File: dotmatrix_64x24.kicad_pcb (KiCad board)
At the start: 2 copper layers, 180 x 100 mm, 369 parts, among them CON1 BARREL_JACK, P1 CONN_01X09, P2 CONN_01X09, P3 CONN_01X04, P4 CONN_01X03, P5 USB_OTG, P6 CONN_01X03, Q1 NJL7302L-F3, SW1 SW_PUSH_SMALL_H, SW2 SW_PUSH_SMALL_H, SW3 SW_PUSH_SMALL_H, SW4 SW_PUSH_SMALL_H, SW5 SW_PUSH_SMALL_H, SW6 SW_PUSH_SMALL_H, SW7 SW_PUSH_SMALL_H, SW8 SW_PUSH_SMALL_H, U1 WROOM-02, U10 LED1642GW, U11 LED1642GW, U12 AE-BME280, U13 OKL-T/6-W5, U14 NJU7223, U15 DS1307, U16 CH340G, U2 74HC595-alt-vdd, U3 TD62783, U4 74HC595-alt-vdd, U5 TD62783, U6 LED1642GW, U7 74HC595-alt-vdd, U8 TD62783, U9 LED1642GW, X1 CRYSTAL_SMD, Y1 12MHz

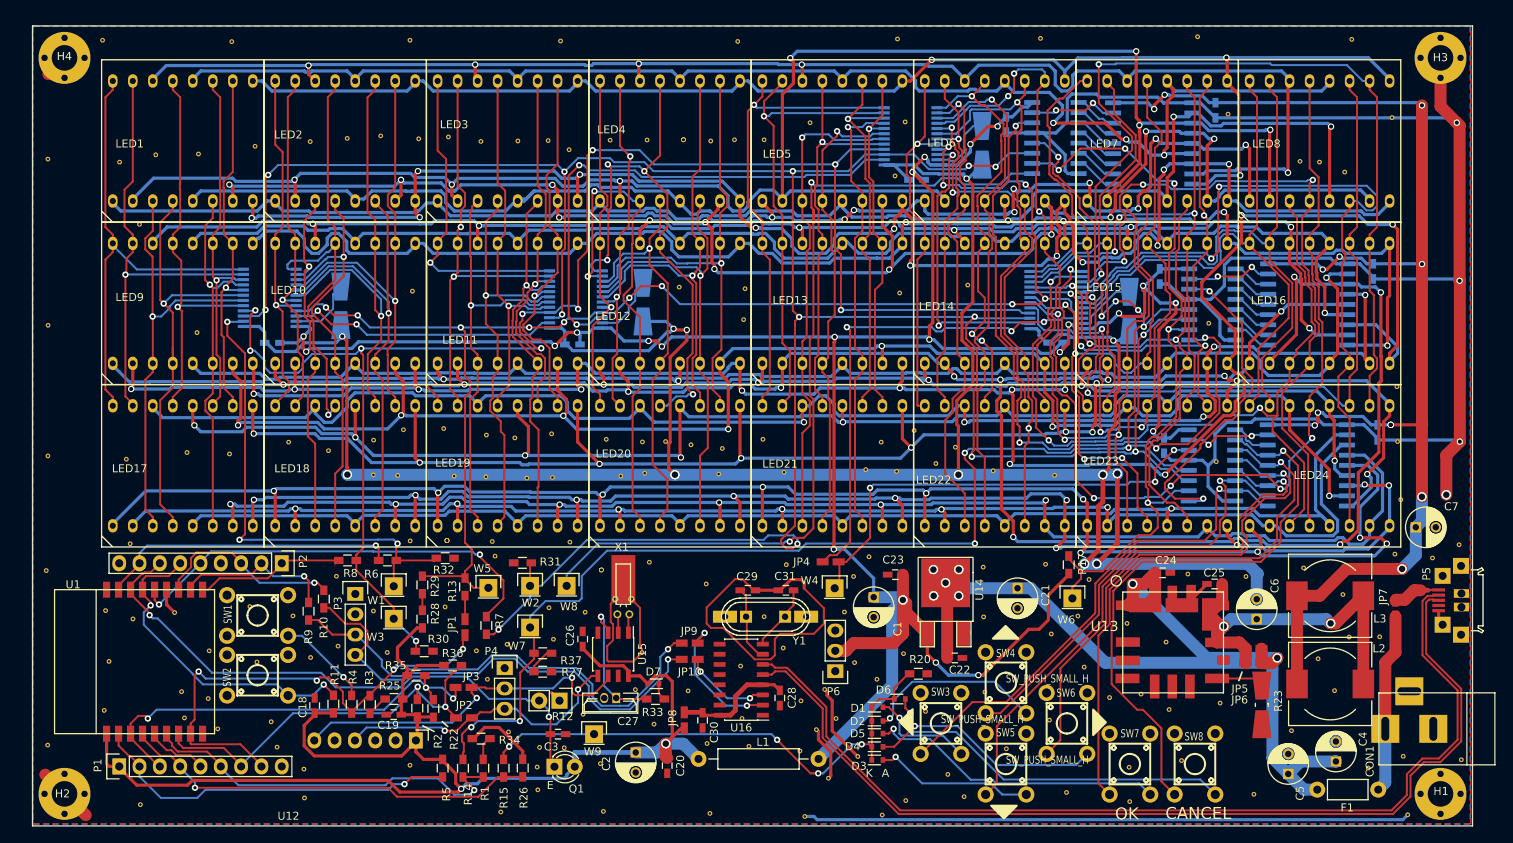
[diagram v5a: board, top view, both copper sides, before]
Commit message: Added IR remote control functionality
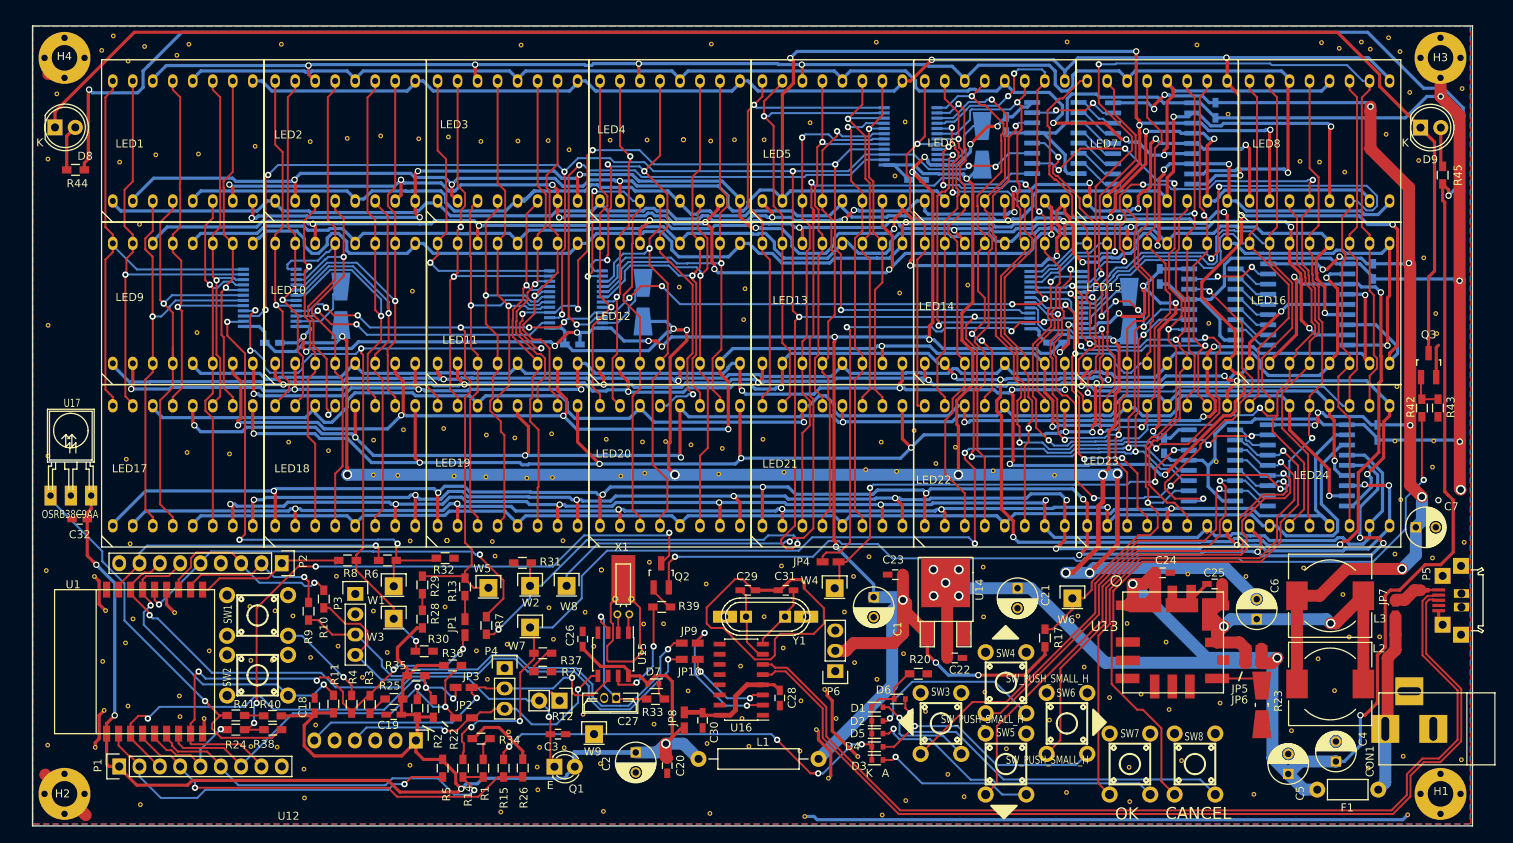
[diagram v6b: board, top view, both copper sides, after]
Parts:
- removed the REF** at (157.6, 13.4)
- removed the REF** at (138.0, 13.6)
- removed the REF** at (120.1, 13.6)
- removed the REF** at (100.2, 13.9)
- removed the REF** at (78.0, 13.9)
- removed the REF** at (59.2, 13.8)
- removed the REF** at (36.9, 14.0)
- removed the REF** at (87.4, 95.0)
- removed the REF** at (34.0, 96.1)
- removed the REF** at (30.6, 95.2)
- removed the REF** at (139.3, 88.0)
- removed the REF** at (144.1, 81.2)
- removed the REF** at (138.6, 79.3)
- added C32: 1u, Capacitors_SMD:C_0603_HandSoldering, F.Cu at (17.9, 73.7)
- added D8: Led_Small, LEDs:LED-5MM, F.Cu at (14.8, 24.7)
- added D9: Led_Small, LEDs:LED-5MM, F.Cu at (185.5, 24.7)
- added Q2: Q_PNP_BEC, TO_SOT_Packages_SMD:SOT-23_Handsoldering, F.Cu at (90.6, 80.7)
- added Q3: Q_NPN_BEC, TO_SOT_Packages_SMD:SOT-23_Handsoldering, F.Cu at (186.5, 54.4)
- added R24: 120R, Resistors_SMD:R_0603_HandSoldering, F.Cu at (37.4, 100.0)
- added R38: 10k, Resistors_SMD:R_0603_HandSoldering, F.Cu at (42.0, 100.0)
- added R39: 1k, Resistors_SMD:R_0603_HandSoldering, F.Cu at (90.7, 84.6)
- added R40: 10k, Resistors_SMD:R_0603_HandSoldering, F.Cu at (42.0, 98.2)
- added R41: 10k, Resistors_SMD:R_0603_HandSoldering, F.Cu at (37.4, 98.2)
- added R42: 1k, Resistors_SMD:R_0603_HandSoldering, F.Cu at (185.7, 59.8)
- added R43: 10k, Resistors_SMD:R_0603_HandSoldering, F.Cu at (187.7, 59.8)
- added R44: 10R, Resistors_SMD:R_0603_HandSoldering, F.Cu at (17.4, 30.0)
- added R45: 10R, Resistors_SMD:R_0603_HandSoldering, F.Cu at (188.3, 30.7)
- added REF**: stitch-via-0.6mm, components:stitch-via-0.6mm, F.Cu at (30.0, 15.7)
- added REF**: stitch-via-0.6mm, components:stitch-via-0.6mm, F.Cu at (19.7, 80.8)
- added REF**: stitch-via-0.6mm, components:stitch-via-0.6mm, F.Cu at (19.8, 102.2)
- added REF**: stitch-via-0.6mm, components:stitch-via-0.6mm, F.Cu at (47.4, 99.4)
- added REF**: stitch-via-0.6mm, components:stitch-via-0.6mm, F.Cu at (187.0, 67.2)
- added REF**: stitch-via-0.6mm, components:stitch-via-0.6mm, F.Cu at (187.4, 48.0)
- added REF**: stitch-via-0.6mm, components:stitch-via-0.6mm, F.Cu at (187.5, 50.5)
- added REF**: stitch-via-0.6mm, components:stitch-via-0.6mm, F.Cu at (187.1, 63.9)
- added REF**: stitch-via-0.6mm, components:stitch-via-0.6mm, F.Cu at (15.0, 20.5)
- added REF**: stitch-via-0.6mm, components:stitch-via-0.6mm, F.Cu at (26.0, 14.6)
- added REF**: stitch-via-0.6mm, components:stitch-via-0.6mm, F.Cu at (43.1, 14.3)
- added REF**: stitch-via-0.6mm, components:stitch-via-0.6mm, F.Cu at (31.5, 14.3)
- added REF**: stitch-via-0.6mm, components:stitch-via-0.6mm, F.Cu at (73.1, 14.4)
- added REF**: stitch-via-0.6mm, components:stitch-via-0.6mm, F.Cu at (96.9, 14.3)
- added REF**: stitch-via-0.6mm, components:stitch-via-0.6mm, F.Cu at (117.5, 14.0)
- added REF**: stitch-via-0.6mm, components:stitch-via-0.6mm, F.Cu at (141.3, 14.0)
- added REF**: stitch-via-0.6mm, components:stitch-via-0.6mm, F.Cu at (157.6, 14.4)
- added REF**: stitch-via-0.6mm, components:stitch-via-0.6mm, F.Cu at (178.1, 14.0)
- added REF**: stitch-via-0.6mm, components:stitch-via-0.6mm, F.Cu at (184.2, 20.3)
- added REF**: stitch-via-0.6mm, components:stitch-via-0.6mm, F.Cu at (185.3, 28.8)
- added REF**: stitch-via-0.6mm, components:stitch-via-0.6mm, F.Cu at (185.9, 41.0)
- added REF**: stitch-via-0.6mm, components:stitch-via-0.6mm, F.Cu at (90.9, 86.7)
- added REF**: stitch-via-0.6mm, components:stitch-via-0.6mm, F.Cu at (190.7, 19.8)
- added REF**: stitch-via-0.6mm, components:stitch-via-0.6mm, F.Cu at (88.4, 86.8)
- added REF**: stitch-via-0.6mm, components:stitch-via-0.6mm, F.Cu at (82.2, 89.6)
- added REF**: stitch-via-0.6mm, components:stitch-via-0.6mm, F.Cu at (42.0, 91.3)
- added REF**: stitch-via-0.6mm, components:stitch-via-0.6mm, F.Cu at (42.3, 85.1)
- added REF**: stitch-via-0.6mm, components:stitch-via-0.6mm, F.Cu at (53.2, 93.4)
- added REF**: stitch-via-0.6mm, components:stitch-via-0.6mm, F.Cu at (30.4, 95.8)
- added REF**: stitch-via-0.6mm, components:stitch-via-0.6mm, F.Cu at (23.9, 97.0)
- added REF**: stitch-via-0.6mm, components:stitch-via-0.6mm, F.Cu at (23.6, 89.1)
- added REF**: stitch-via-0.6mm, components:stitch-via-0.6mm, F.Cu at (175.3, 14.8)
- added REF**: stitch-via-0.6mm, components:stitch-via-0.6mm, F.Cu at (173.1, 14.1)
- added REF**: stitch-via-0.6mm, components:stitch-via-0.6mm, F.Cu at (179.2, 14.9)
- added REF**: stitch-via-0.6mm, components:stitch-via-0.6mm, F.Cu at (182.9, 15.2)
- added REF**: stitch-via-0.6mm, components:stitch-via-0.6mm, F.Cu at (24.0, 16.4)
- added REF**: stitch-via-0.6mm, components:stitch-via-0.6mm, F.Cu at (22.1, 13.3)
- added U17: OSRB38C9AA, components:IRM2161_LAY, F.Cu at (16.8, 70.7)
- moved R17 9.63 mm to (138.6, 88.5)
- moved REF** 4.60 mm to (181.5, 13.5)
- moved REF** 4.01 mm to (39.3, 102.1)
- moved REF** 2.21 mm to (181.2, 25.6)
- moved REF** 2.14 mm to (33.5, 98.6)
- moved REF** 1.27 mm to (20.7, 15.1)
- moved REF** 0.88 mm to (78.3, 76.4)
- moved REF** 0.79 mm to (39.3, 91.3)
- moved REF** 0.79 mm to (20.8, 91.4)
- moved REF** 0.70 mm to (191.0, 76.6)
- moved REF** 0.63 mm to (105.6, 79.5)
- moved REF** 0.58 mm to (30.4, 98.3)
- moved REF** 0.33 mm to (182.3, 63.9)
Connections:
- U15 pad 7: Net-(U15-Pad7) -> /#IR_LED_EN
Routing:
- net VCC: track 155.4 -> 441.0 mm, vias 7 -> 10
- net /IR_LED_DRIVE: track 0.00 -> 211.8 mm
- net Net-(Q2-Pad2): track 0.00 -> 114.5 mm, vias 0 -> 2
- net /IR: track 0.00 -> 78.2 mm, vias 0 -> 4
- net Net-(R38-Pad2): track 0.00 -> 48.8 mm, vias 0 -> 1
- net /ESPVDD: track 169.7 -> 205.8 mm, vias 2 -> 4
- net GND: track 744.1 -> 762.1 mm
- net /#IR_LED_EN: track 0.00 -> 13.9 mm, vias 0 -> 2
- net /LEDLOGICVDD: track 322.0 -> 313.1 mm
- net /Sheet57A04605/LEDVDD: track 167.3 -> 160.2 mm, vias 12 -> 11
- net Net-(P1-Pad5): track 7.85 -> 14.4 mm, vias 0 -> 1
- net Net-(D8-Pad2): track 0.00 -> 5.75 mm
- net Net-(D9-Pad2): track 0.00 -> 4.94 mm
- net Net-(Q3-Pad1): track 0.00 -> 4.81 mm
- net Net-(Q2-Pad1): track 0.00 -> 3.42 mm
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
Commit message: Fixed electrolyric capacitor diameter
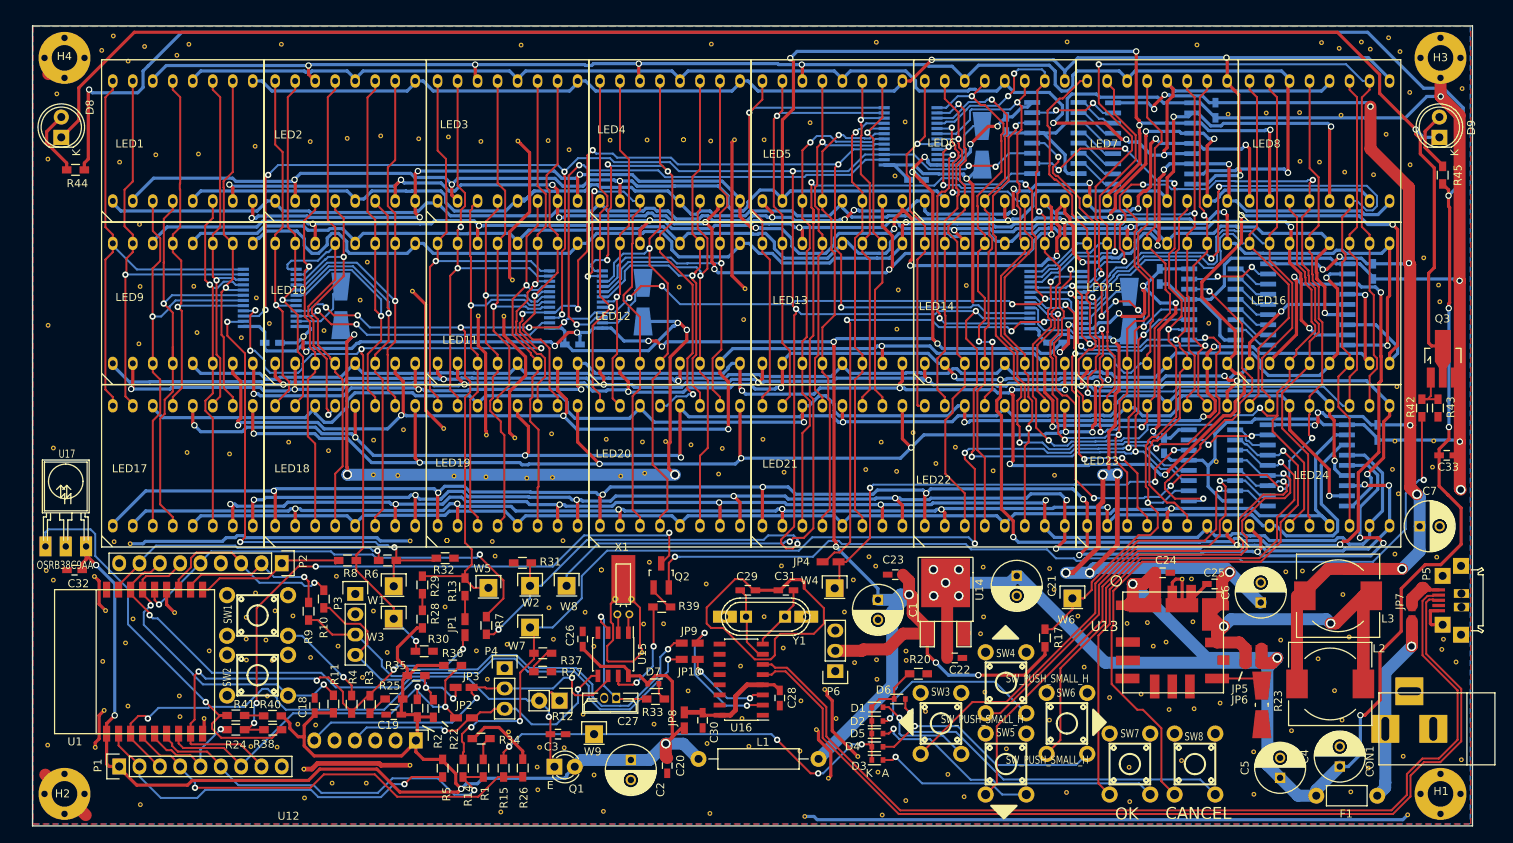
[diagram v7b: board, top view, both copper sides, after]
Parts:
- removed the REF** at (156.4, 80.5)
- removed the REF** at (163.7, 80.8)
- added C33: 1u, Capacitors_SMD:C_0603_HandSoldering, F.Cu at (188.8, 65.7)
- added REF**: stitch-via-0.6mm, components:stitch-via-0.6mm, F.Cu at (41.2, 88.8)
- added REF**: stitch-via-0.6mm, components:stitch-via-0.6mm, F.Cu at (22.2, 76.5)
- added REF**: stitch-via-0.6mm, components:stitch-via-0.6mm, F.Cu at (117.5, 91.2)
- added REF**: stitch-via-0.6mm, components:stitch-via-0.6mm, F.Cu at (121.2, 91.3)
- added REF**: stitch-via-0.6mm, components:stitch-via-0.6mm, F.Cu at (117.4, 79.5)
- added REF**: stitch-via-0.6mm, components:stitch-via-0.6mm, F.Cu at (188.2, 89.9)
- added REF**: stitch-via-0.6mm, components:stitch-via-0.6mm, F.Cu at (189.9, 91.5)
- added REF**: stitch-via-0.6mm, components:stitch-via-0.6mm, F.Cu at (176.8, 107.7)
- added REF**: stitch-via-0.6mm, components:stitch-via-0.6mm, F.Cu at (175.7, 98.8)
- added REF**: stitch-via-0.6mm, components:stitch-via-0.6mm, F.Cu at (164.6, 102.7)
- added REF**: stitch-via-0.6mm, components:stitch-via-0.6mm, F.Cu at (168.0, 88.8)
- added REF**: stitch-via-0.6mm, components:stitch-via-0.6mm, F.Cu at (38.7, 88.6)
- added REF**: stitch-via-0.6mm, components:stitch-via-0.6mm, F.Cu at (157.2, 97.4)
- added REF**: stitch-via-0.6mm, components:stitch-via-0.6mm, F.Cu at (152.1, 89.5)
- added REF**: stitch-via-0.6mm, components:stitch-via-0.6mm, F.Cu at (157.0, 86.5)
- added REF**: stitch-via-0.6mm, components:stitch-via-0.6mm, F.Cu at (151.4, 86.6)
- added REF**: stitch-via-0.6mm, components:stitch-via-0.6mm, F.Cu at (130.5, 88.0)
- added REF**: stitch-via-0.6mm, components:stitch-via-0.6mm, F.Cu at (67.7, 48.3)
- added REF**: stitch-via-0.6mm, components:stitch-via-0.6mm, F.Cu at (70.9, 48.3)
- added REF**: stitch-via-0.6mm, components:stitch-via-0.6mm, F.Cu at (53.8, 41.5)
- added REF**: stitch-via-0.6mm, components:stitch-via-0.6mm, F.Cu at (41.6, 49.2)
- added REF**: stitch-via-0.6mm, components:stitch-via-0.6mm, F.Cu at (48.4, 50.1)
- added REF**: stitch-via-0.6mm, components:stitch-via-0.6mm, F.Cu at (38.7, 85.9)
- added REF**: stitch-via-0.6mm, components:stitch-via-0.6mm, F.Cu at (38.1, 51.0)
- added REF**: stitch-via-0.6mm, components:stitch-via-0.6mm, F.Cu at (40.0, 46.0)
- added REF**: stitch-via-0.6mm, components:stitch-via-0.6mm, F.Cu at (25.3, 51.7)
- added REF**: stitch-via-0.6mm, components:stitch-via-0.6mm, F.Cu at (32.2, 44.6)
- added REF**: stitch-via-0.6mm, components:stitch-via-0.6mm, F.Cu at (25.5, 44.6)
- added REF**: stitch-via-0.6mm, components:stitch-via-0.6mm, F.Cu at (120.0, 49.9)
- added REF**: stitch-via-0.6mm, components:stitch-via-0.6mm, F.Cu at (53.0, 46.3)
- added REF**: stitch-via-0.6mm, components:stitch-via-0.6mm, F.Cu at (41.4, 95.8)
- added REF**: stitch-via-0.6mm, components:stitch-via-0.6mm, F.Cu at (45.2, 99.3)
- added REF**: stitch-via-0.6mm, components:stitch-via-0.6mm, F.Cu at (53.7, 106.7)
- added REF**: stitch-via-0.6mm, components:stitch-via-0.6mm, F.Cu at (72.0, 43.8)
- added REF**: stitch-via-0.6mm, components:stitch-via-0.6mm, F.Cu at (49.5, 106.7)
- added REF**: stitch-via-0.6mm, components:stitch-via-0.6mm, F.Cu at (117.7, 105.3)
- added REF**: stitch-via-0.6mm, components:stitch-via-0.6mm, F.Cu at (175.6, 23.2)
- added REF**: stitch-via-0.6mm, components:stitch-via-0.6mm, F.Cu at (170.4, 22.8)
- added REF**: stitch-via-0.6mm, components:stitch-via-0.6mm, F.Cu at (166.2, 22.9)
- added REF**: stitch-via-0.6mm, components:stitch-via-0.6mm, F.Cu at (179.6, 30.6)
- added REF**: stitch-via-0.6mm, components:stitch-via-0.6mm, F.Cu at (155.7, 81.2)
- added REF**: stitch-via-0.6mm, components:stitch-via-0.6mm, F.Cu at (156.9, 81.1)
- added REF**: stitch-via-0.6mm, components:stitch-via-0.6mm, F.Cu at (139.1, 79.8)
- added REF**: stitch-via-0.6mm, components:stitch-via-0.6mm, F.Cu at (139.7, 82.4)
- added REF**: stitch-via-0.6mm, components:stitch-via-0.6mm, F.Cu at (168.7, 80.2)
- C1, C2, C21, C4, C5, C6, C7: footprint Capacitors_ThroughHole:C_Radial_D5_L6_P2.5 -> Capacitors_ThroughHole:C_Radial_D6.3_L11.2_P2.5
- Q2: value Q_PNP_BEC -> Q_PNP_BEC 2SA1162
- Q3: value Q_NPN_BEC -> Q_NPN_BCE RN5006; footprint TO_SOT_Packages_SMD:SOT-23_Handsoldering -> TO_SOT_Packages_SMD:SOT89-3_Housing_Handsoldering
- moved REF** 15.5 mm to (14.6, 81.3)
- moved REF** 12.8 mm to (182.0, 67.4)
- moved REF** 9.22 mm to (14.6, 64.8)
- moved REF** 7.98 mm to (188.4, 88.7)
- moved C32 6.38 mm to (17.3, 80.0)
- moved U17 6.38 mm to (16.2, 77.1)
- moved REF** 4.01 mm to (187.9, 46.5)
- moved REF** 3.57 mm to (187.8, 44.4)
- moved D9 2.66 mm to (187.9, 25.9), turned to 90 degrees
- moved C6 2.14 mm to (165.5, 84.1)
- moved JP7 2.14 mm to (184.4, 85.4)
- moved Q3 1.95 mm to (188.3, 53.6)
- moved REF** 1.84 mm to (39.9, 82.9)
- moved REF** 1.63 mm to (82.2, 105.6)
- moved C21 1.55 mm to (135.0, 80.7)
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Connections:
- Q3 pad 2: GND -> /IR_LED_DRIVE
- Q3 pad 3: /IR_LED_DRIVE -> GND
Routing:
- net Net-(C25-Pad1): track 45.5 -> 116.5 mm, vias 2 -> 7
- net /Sheet57A04605/LEDVDD: track 160.2 -> 175.5 mm
- net GND: track 762.1 -> 776.0 mm, vias 16 -> 11
- net /IR_LED_DRIVE: track 211.8 -> 220.7 mm, vias 0 -> 1
- net /ESPVDD: track 205.8 -> 201.4 mm
- net Net-(D9-Pad2): track 4.94 -> 8.14 mm
- net /Sheet57A04605/c38: track 48.2 -> 45.4 mm
- net /Sheet57A04605/c39: track 58.5 -> 55.8 mm
- net Net-(D8-Pad2): track 5.75 -> 8.40 mm
- net Net-(R38-Pad2): track 48.8 -> 51.5 mm
- net /Sheet57A04605/c17: track 48.3 -> 50.5 mm
- net /Sheet57A04605/c25: track 69.9 -> 71.7 mm
- net /DC_IN: track 22.5 -> 24.3 mm, vias 0 -> 1
- net /Sheet57A04605/COLCLK: track 337.5 -> 339.0 mm
- net /Sheet57A04605/c37: track 56.9 -> 55.5 mm
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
